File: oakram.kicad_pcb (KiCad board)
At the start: 2 copper layers, 4 parts, among them U1 DRAM_1MX16_SOJ, U2 DRAM_1MX16_SOJ, X1 ZIP40, X2 ZIP40

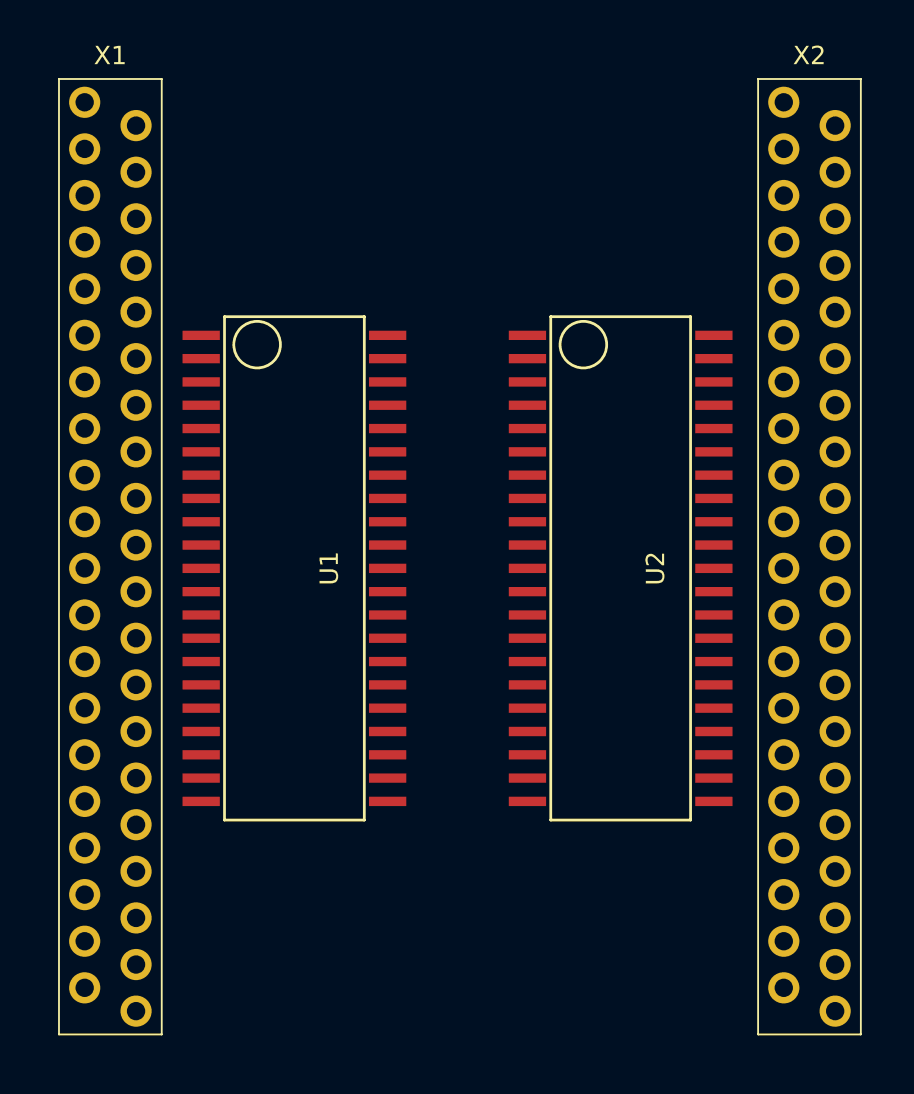
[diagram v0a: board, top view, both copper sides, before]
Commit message: Some bus signals assigned
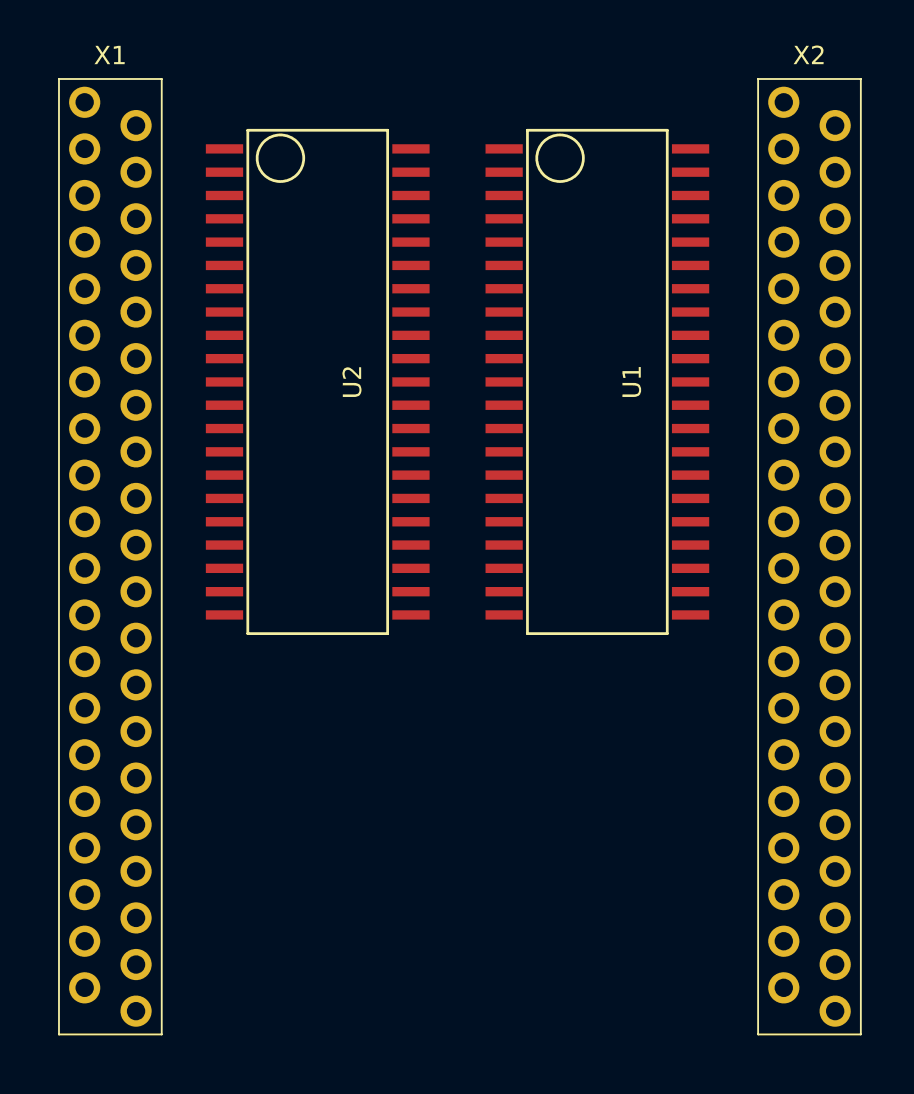
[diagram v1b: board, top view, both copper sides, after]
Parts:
- moved U1 19.4 mm to (149.9, 91.4)
- moved U2 19.4 mm to (134.6, 91.4)
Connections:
- U1 pad 10: Net-(U1-Pad10) -> /D23
- U1 pad 17: Net-(U1-Pad17) -> /A0
- U1 pad 18: Net-(U1-Pad18) -> /A1
- U1 pad 19: Net-(U1-Pad19) -> /A2
- U1 pad 2: Net-(U1-Pad2) -> /D16
- U1 pad 20: Net-(U1-Pad20) -> /A3
- U1 pad 23: Net-(U1-Pad23) -> /A4
- U1 pad 24: Net-(U1-Pad24) -> /A5
- U1 pad 25: Net-(U1-Pad25) -> /A6
- U1 pad 26: Net-(U1-Pad26) -> /A7
- U1 pad 27: Net-(U1-Pad27) -> /A8
- U1 pad 28: Net-(U1-Pad28) -> /A9
- U1 pad 3: Net-(U1-Pad3) -> /D17
- U1 pad 33: Net-(U1-Pad33) -> /D24
- U1 pad 34: Net-(U1-Pad34) -> /D25
- U1 pad 35: Net-(U1-Pad35) -> /D26
- U1 pad 36: Net-(U1-Pad36) -> /D27
- U1 pad 38: Net-(U1-Pad38) -> /D28
- U1 pad 39: Net-(U1-Pad39) -> /D29
- U1 pad 4: Net-(U1-Pad4) -> /D18
- U1 pad 40: Net-(U1-Pad40) -> /D30
- U1 pad 41: Net-(U1-Pad41) -> /D31
- U1 pad 5: Net-(U1-Pad5) -> /D19
- U1 pad 7: Net-(U1-Pad7) -> /D20
- U1 pad 8: Net-(U1-Pad8) -> /D21
- U1 pad 9: Net-(U1-Pad9) -> /D22
- U2 pad 10: Net-(U2-Pad10) -> /D7
- U2 pad 17: Net-(U2-Pad17) -> /A0
- U2 pad 18: Net-(U2-Pad18) -> /A1
- U2 pad 19: Net-(U2-Pad19) -> /A2
- U2 pad 2: Net-(U2-Pad2) -> /D0
- U2 pad 20: Net-(U2-Pad20) -> /A3
- U2 pad 23: Net-(U2-Pad23) -> /A4
- U2 pad 24: Net-(U2-Pad24) -> /A5
- U2 pad 25: Net-(U2-Pad25) -> /A6
- U2 pad 26: Net-(U2-Pad26) -> /A7
- U2 pad 27: Net-(U2-Pad27) -> /A8
- U2 pad 28: Net-(U2-Pad28) -> /A9
- U2 pad 3: Net-(U2-Pad3) -> /D1
- U2 pad 33: Net-(U2-Pad33) -> /D8
- U2 pad 34: Net-(U2-Pad34) -> /D9
- U2 pad 35: Net-(U2-Pad35) -> /D10
- U2 pad 36: Net-(U2-Pad36) -> /D11
- U2 pad 38: Net-(U2-Pad38) -> /D12
- U2 pad 39: Net-(U2-Pad39) -> /D13
- U2 pad 4: Net-(U2-Pad4) -> /D2
- U2 pad 40: Net-(U2-Pad40) -> /D14
- U2 pad 41: Net-(U2-Pad41) -> /D15
- U2 pad 5: Net-(U2-Pad5) -> /D3
- U2 pad 7: Net-(U2-Pad7) -> /D4
- U2 pad 8: Net-(U2-Pad8) -> /D5
- U2 pad 9: Net-(U2-Pad9) -> /D6

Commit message: Moar
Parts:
- U1, U2: value DRAM_1MX16_SOJ -> IS41C16105C
- moved U1 10.2 mm to (148.6, 101.6)
- moved U2 10.2 mm to (133.3, 101.6)
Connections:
- U1 pad 10: /D23 -> /D31
- U1 pad 13: Net-(U1-Pad13) -> /~WE
- U1 pad 14: Net-(U1-Pad14) -> /~RAS
- U1 pad 2: /D16 -> /D24
- U1 pad 29: Net-(U1-Pad29) -> /~OE
- U1 pad 3: /D17 -> /D25
- U1 pad 30: Net-(U1-Pad30) -> /~CAS3
- U1 pad 31: Net-(U1-Pad31) -> /~CAS2
- U1 pad 33: /D24 -> /D23
- U1 pad 34: /D25 -> /D22
- U1 pad 35: /D26 -> /D21
- U1 pad 36: /D27 -> /D20
- U1 pad 38: /D28 -> /D19
- U1 pad 39: /D29 -> /D18
- U1 pad 4: /D18 -> /D26
- U1 pad 40: /D30 -> /D17
- U1 pad 41: /D31 -> /D16
- U1 pad 5: /D19 -> /D27
- U1 pad 7: /D20 -> /D28
- U1 pad 8: /D21 -> /D29
- U1 pad 9: /D22 -> /D30
- U2 pad 13: Net-(U2-Pad13) -> /~WE
- U2 pad 14: Net-(U2-Pad14) -> /~RAS
- U2 pad 29: Net-(U2-Pad29) -> /~OE
- U2 pad 30: Net-(U2-Pad30) -> /~CAS1
- U2 pad 31: Net-(U2-Pad31) -> /~CAS0
- U2 pad 33: /D8 -> /D15
- U2 pad 34: /D9 -> /D14
- U2 pad 35: /D10 -> /D13
- U2 pad 36: /D11 -> /D12
- U2 pad 38: /D12 -> /D11
- U2 pad 39: /D13 -> /D10
- U2 pad 40: /D14 -> /D9
- U2 pad 41: /D15 -> /D8
- X1 pad 11: +5VDC -> VCC
- X1 pad 16: +5VDC -> VCC
- X1 pad 30: +5VDC -> VCC
- X2 pad 11: +5VDC -> VCC
- X2 pad 16: +5VDC -> VCC
- X2 pad 30: +5VDC -> VCC
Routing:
- net /~WE: track 0.00 -> 39.0 mm
- net /D28: track 0.00 -> 28.4 mm
- net /D30: track 0.00 -> 28.4 mm
- net /D27: track 0.00 -> 27.7 mm
- net /D25: track 0.00 -> 27.7 mm
- net /A9: track 0.00 -> 26.7 mm
- net /D29: track 0.00 -> 25.6 mm
- net /D31: track 0.00 -> 25.6 mm
- net /D13: track 0.00 -> 25.6 mm
- net /D15: track 0.00 -> 25.6 mm
- net /D26: track 0.00 -> 24.9 mm
- net /D24: track 0.00 -> 24.9 mm
- net /D8: track 0.00 -> 24.5 mm
- net /D10: track 0.00 -> 24.5 mm
- net /D14: track 0.00 -> 22.8 mm
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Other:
- net class Default: clearance 0 -> 0.15
- rule trace_clearance: 0 -> 0.15

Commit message: Up
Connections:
- X1 pad 32: /A4 -> Net-(X1-Pad32)
- X1 pad 33: /A5 -> Net-(X1-Pad33)
- X1 pad 34: /A6 -> Net-(X1-Pad34)
- X1 pad 35: /A7 -> Net-(X1-Pad35)
- X1 pad 36: /A8 -> Net-(X1-Pad36)
- X2 pad 22: /A9 -> Net-(X2-Pad22)
- X2 pad 23: /~WE -> Net-(X2-Pad23)
- X2 pad 24: /~RAS -> Net-(X2-Pad24)
- X2 pad 26: /A0 -> Net-(X2-Pad26)
- X2 pad 27: /A1 -> Net-(X2-Pad27)
- X2 pad 28: /A2 -> Net-(X2-Pad28)
- X2 pad 29: /A3 -> Net-(X2-Pad29)
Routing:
- net /~CAS0: track 0.00 -> 34.8 mm, vias 0 -> 1
- net /~CAS3: track 0.00 -> 31.4 mm
- net /~CAS1: track 0.00 -> 28.8 mm, vias 0 -> 1
- net /~CAS2: track 0.00 -> 26.1 mm
- net /A8: track 15.8 -> 39.1 mm, vias 0 -> 1
- net /A7: track 15.8 -> 33.5 mm, vias 0 -> 1
- net /A6: track 15.8 -> 33.5 mm, vias 0 -> 1
- net /~WE: track 39.0 -> 22.1 mm
- net /A5: track 15.8 -> 27.9 mm, vias 0 -> 1
- net /A4: track 15.8 -> 27.9 mm, vias 0 -> 1
- net VSS: track 8.26 -> 0.00 mm, vias 5 -> 0
- net /A9: track 26.7 -> 33.4 mm, vias 0 -> 2
- net VCC: track 8.89 -> 14.0 mm
- added copper zone on B.Cu, net GND
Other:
- net class Default: via_dia 0.7 -> 0.8; via_drill 0.3 -> 0.4
- rule via_min_drill: 0.3 -> 0.4
- rule via_min_size: 0.4 -> 0.8

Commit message: Added caps
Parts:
- added C1: 2,2u, Capacitors_SMD:C_0805, F.Cu at (129.5, 116.2)
- added C2: 2,2u, Capacitors_SMD:C_0805, B.Cu at (130.2, 97.2)
- added C3: 2,2u, Capacitors_SMD:C_0805, F.Cu at (144.8, 116.2)
- added C4: 2,2u, Capacitors_SMD:C_0805, B.Cu at (141.6, 97.2)
- added C5: 2,2u, Capacitors_SMD:C_0805, B.Cu at (129.5, 90.2)
- added C6: 2,2u, Capacitors_SMD:C_0805, F.Cu at (141.0, 87.6)
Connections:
- U1 pad 30: /~CAS3 -> /~CAS2
- U1 pad 31: /~CAS2 -> /~CAS3
- X1 pad 10: GND -> VSS
- X1 pad 31: GND -> VSS
- X1 pad 5: GND -> VSS
- X2 pad 10: GND -> VSS
- X2 pad 31: GND -> VSS
- X2 pad 5: GND -> VSS
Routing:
- net VSS: track 0.00 -> 123.4 mm, vias 0 -> 27
- net /~OE: track 0.00 -> 59.7 mm, vias 0 -> 3
- net /~CAS3: track 31.4 -> 27.2 mm
- net /~CAS2: track 26.1 -> 24.4 mm
- net VCC: track 14.0 -> 15.3 mm
- net /~CAS0: track 34.8 -> 33.6 mm
- added copper zone on B.Cu, net VCC
- added copper zone on B.Cu, net VSS
- added copper zone on F.Cu, net VSS
- removed copper zone on B.Cu, net GND
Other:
- net class Default: clearance 0.15 -> 0
- rule trace_clearance: 0.15 -> 0
